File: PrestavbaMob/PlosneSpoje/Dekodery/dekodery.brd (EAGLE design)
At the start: 100 x 80 mm, 30 parts, among them CON1 MLW06_90°, IC1 ATMEGA48/88/168-AU, Q2 Q_HC-49U_SMD, T1 BUZ11, T2 BUZ11

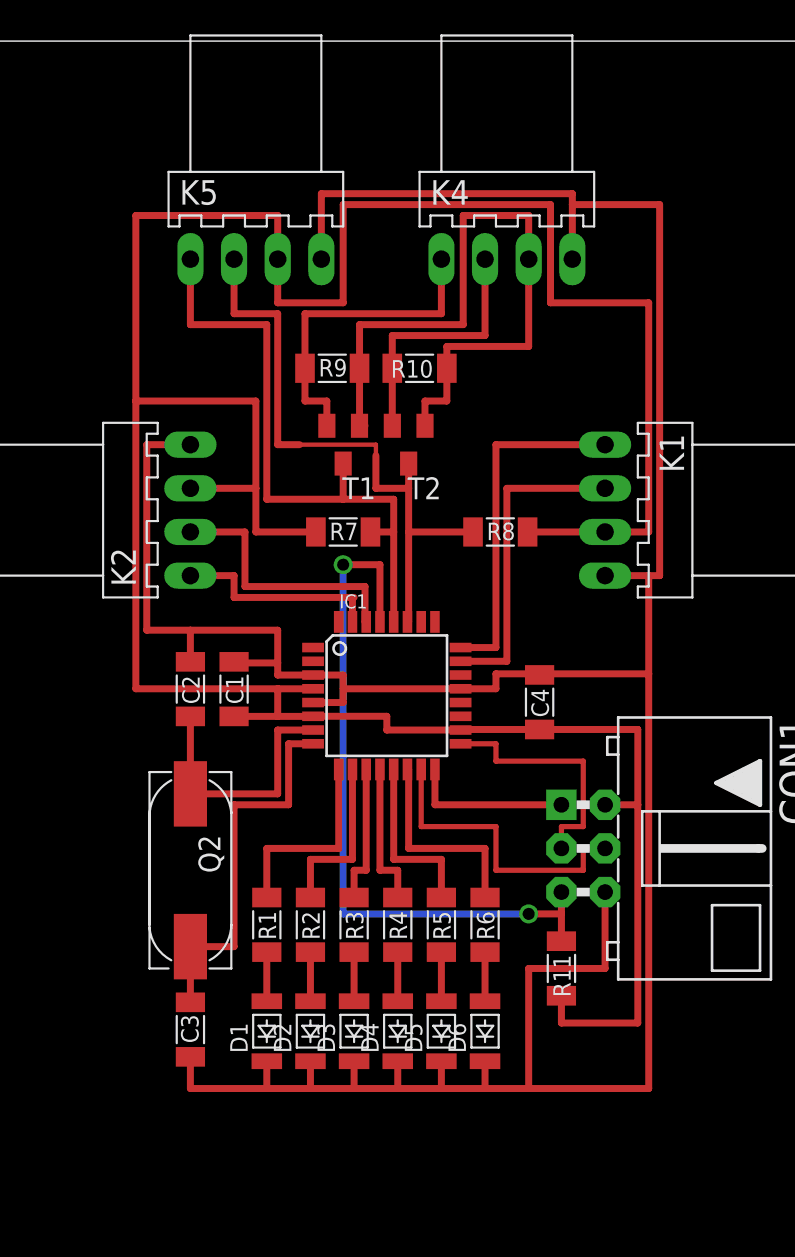
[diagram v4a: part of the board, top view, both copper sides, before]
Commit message: Hotova verze desky rev.1 otestovana a napajena. Nepatrne upravy v kodu.
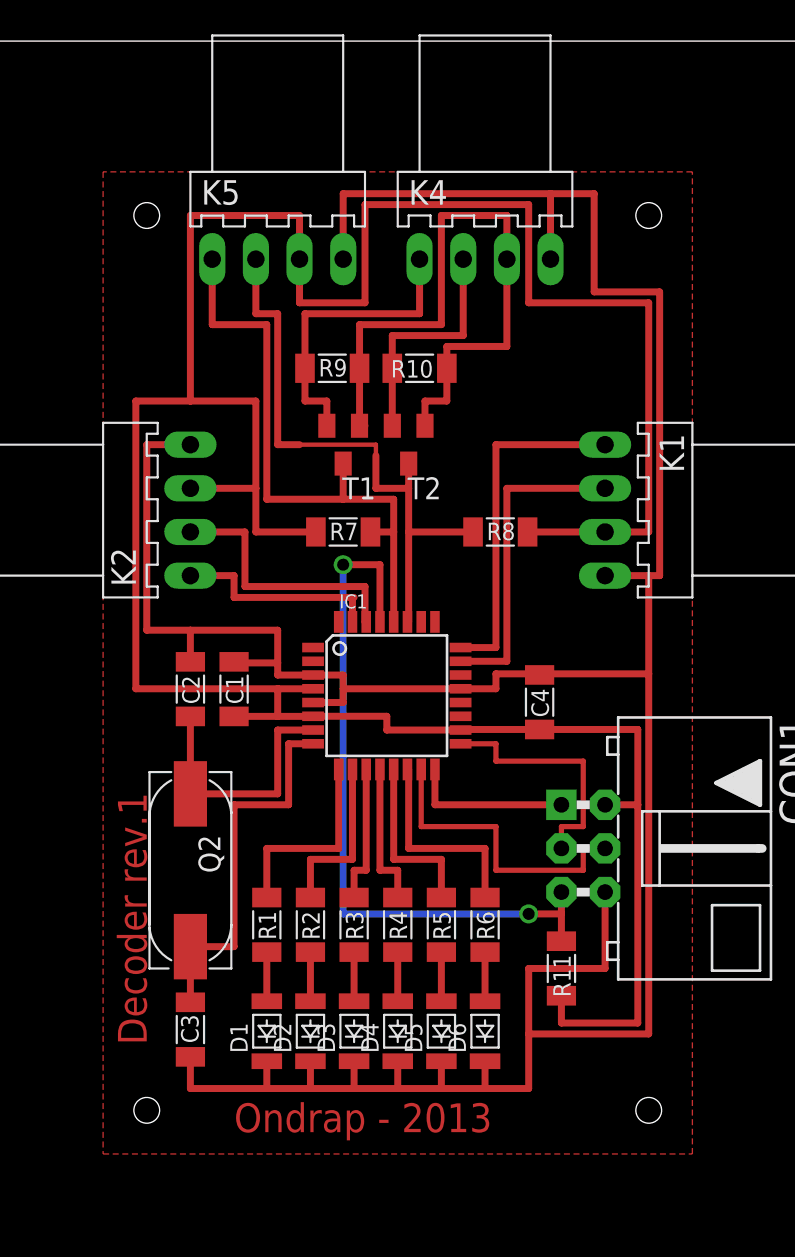
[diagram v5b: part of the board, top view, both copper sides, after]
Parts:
- moved K4 1.27 mm to (34.9, 67.3)
- moved K5 1.27 mm to (22.9, 67.3)
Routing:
- net GND: track 189.7 -> 185.8 mm
- net VCC: track 177.5 -> 174.3 mm
- net N$24: track 41.9 -> 39.4 mm
- net N$5: track 36.4 -> 35.1 mm
- net N$23: track 36.5 -> 35.3 mm
- net N$27: track 19.2 -> 18.0 mm
- net N$26: track 15.1 -> 13.8 mm
- added copper zone on layer 1, net GND
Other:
- board text added: "Decoder rev.1"
- board text added: "Ondrap - 2013"
